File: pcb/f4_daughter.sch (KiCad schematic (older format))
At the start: 0 parts

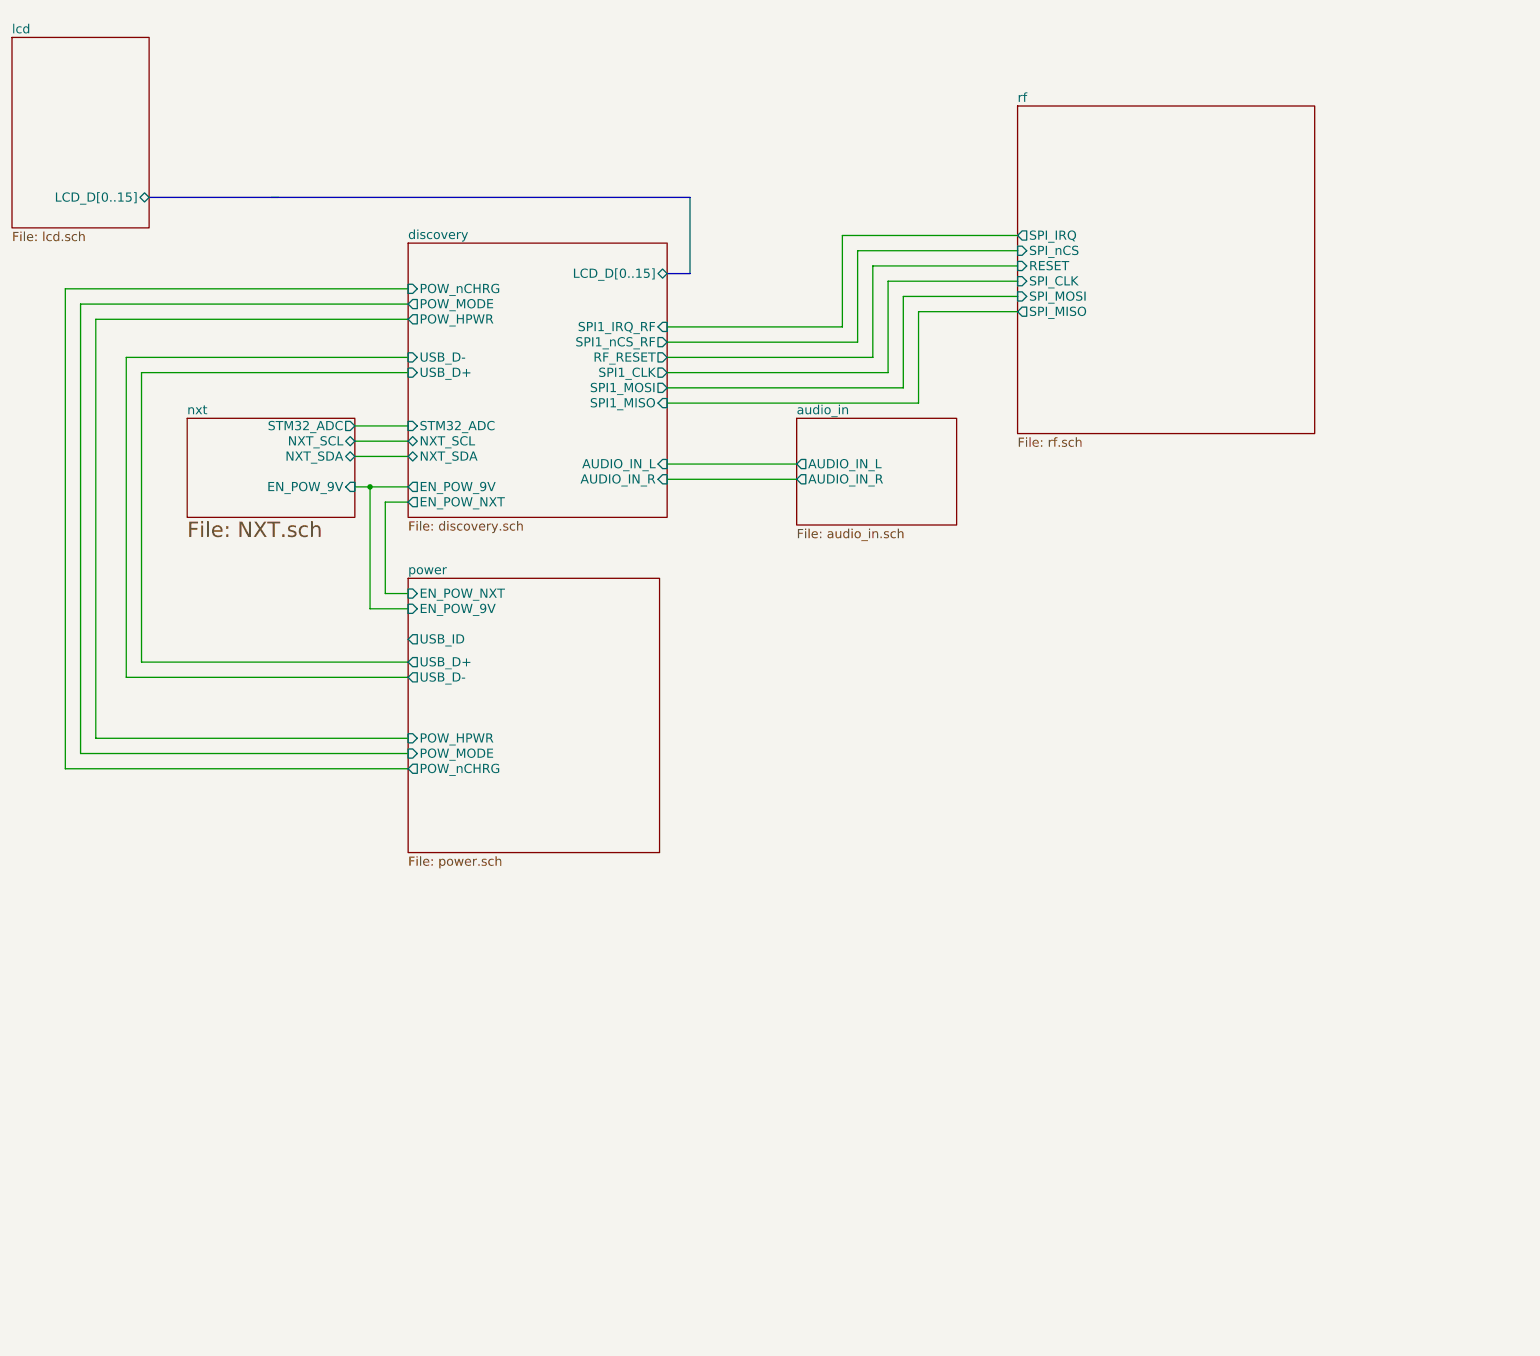
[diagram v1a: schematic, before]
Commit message: A few things: Remapped all interrupts and identified unusable pins on board Added all required connections for LCD and company Added pull-down resistor on STM32W Renamed some internal signals on RF for consistency
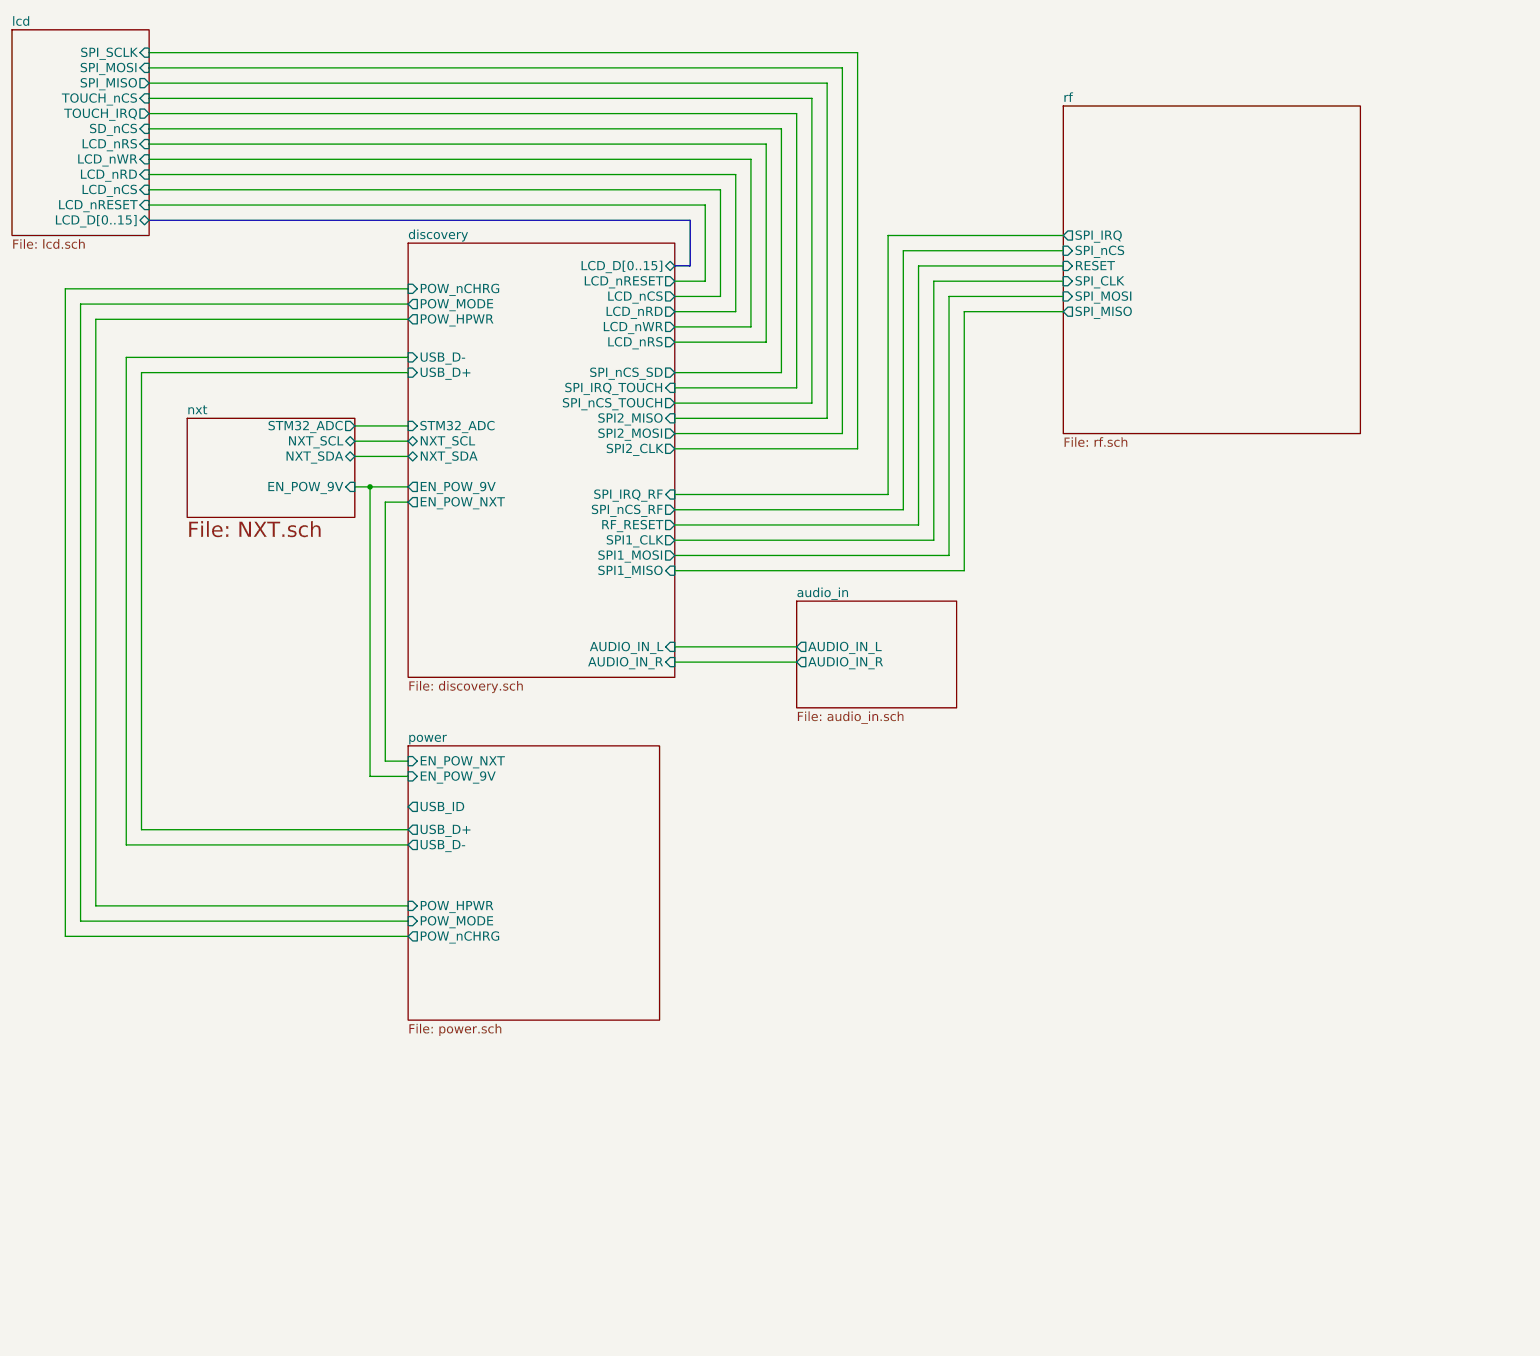
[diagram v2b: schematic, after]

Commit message: Changed some values and connected more LCD signals
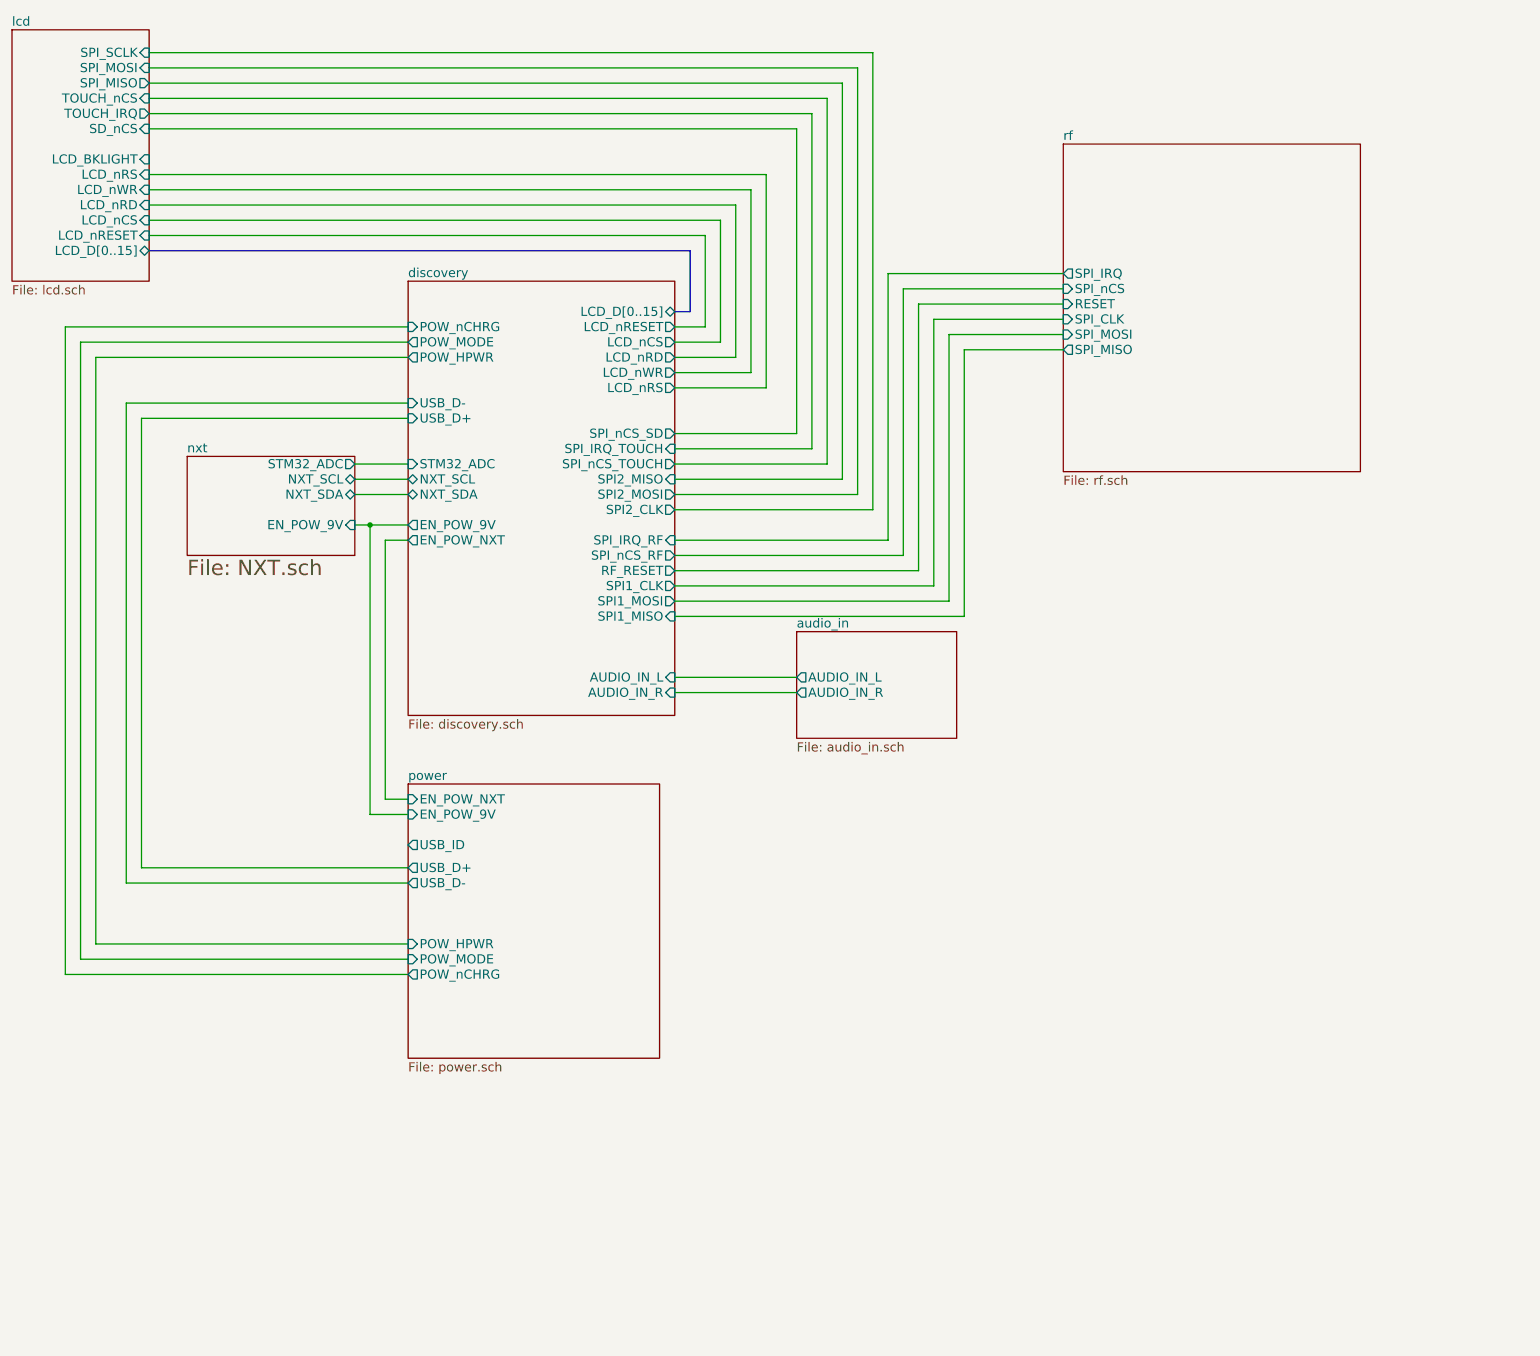
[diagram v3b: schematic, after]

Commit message: Added CPLD, CPLD doc, and backlight driver doc
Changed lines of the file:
@@
-EESchema Schematic File Version 2  date Sun 28 Oct 2012 06:31:28 PM EDT
+EESchema Schematic File Version 2  date Thu 06 Dec 2012 03:45:08 PM EST
 LIBS:power
 LIBS:device
@@
 Sheet 1 7
 Title ""
-Date "28 oct 2012"
+Date "6 dec 2012"
 Rev ""
 Comp ""
@@
 	3600 3700 3950 3700
 Wire Wire Line
-	3600 3900 3950 3900
+	3600 3900 3700 3900
+Wire Wire Line
+	3700 3900 3950 3900
 Wire Wire Line
 	2200 6150 2200 3200

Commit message: Started moving things around for CPLD
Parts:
- added S? (x4): EVQ-Q2S03W, symbol EVQ-Q2S03W
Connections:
- net labels added: GND, S1, S2, S3, S4
- wire segments 78 -> 97

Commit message: finished CPLD schematic and started adding new discovery sheet
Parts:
- removed S? (x4): EVQ-Q2S03W, symbol EVQ-Q2S03W
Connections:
- net labels removed: GND, S1, S2, S3, S4
- wire segments 97 -> 81
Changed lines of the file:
@@
-EESchema Schematic File Version 2  date Thu 06 Dec 2012 06:44:11 PM EST
+EESchema Schematic File Version 2  date 12/12/2012 5:26:02 PM
 LIBS:power
 LIBS:device
@@
 $Descr A4 11700 8267
 encoding utf-8
-Sheet 1 8
+Sheet 1 10
 Title ""
-Date "6 dec 2012"
+Date "12 dec 2012"
 Rev ""
 Comp ""
@@
 Comment4 ""
 $EndDescr
+$Sheet
+S 7900 4700 1700 4450
+U 50C8AECE
+F0 "CPLD" 60
+F1 "CPLD.sch" 60
+F2 "POW_HPWR" O R 9600 4800 60
+F3 "POW_NXT" O R 9600 4900 60
+F4 "POW_MODE" O R 9600 5000 60
+F5 "POW_9V" O R 9600 5100 60
+F6 "POW_MULT0" I L 7900 5050 60
+F7 "POW_MULT1" I L 7900 5150 60
+F8 "POW_MULT2" I L 7900 5250 60
+F9 "FSMC_A16" I L 7900 5450 60
+F10 "FSMC_NWE" I L 7900 5550 60
+F11 "FSMC_NEx" I L 7900 5650 60
+F12 "EXTI0" O L 7900 5800 60
+F13 "EXTI1" O L 7900 5900 60
+F14 "EXTI2" O L 7900 6000 60
+F15 "EXTI3" O L 7900 6100 60
+F16 "EXTI4" O L 7900 6200 60
+F17 "EXTI5" O L 7900 6300 60
+F18 "EXTI9" O L 7900 6400 60
+F19 "EXTI8" O L 7900 6500 60
+F20 "EXTI7" O L 7900 6600 60
+F21 "EXTI6" O L 7900 6700 60
+F22 "SPI_MISO" O R 9600 5350 60
+F23 "SPI_NCS" I R 9600 5450 60
+F24 "SPI_MOSI" I R 9600 5550 60
+F25 "SPI_SCK" I R 9600 5650 60
+F26 "RS" O R 9600 5800 60
+F27 "nWR" O R 9600 5900 60
+F28 "nRD" O R 9600 6000 60
+F29 "nCS" O R 9600 6150 60
+F30 "TOUCH_IRQ" I R 9600 6300 60
+F31 "RF_IRQ" I R 9600 6350 60
+F32 "DEN_GYR" I R 9600 6500 60
+F33 "INT2_GYR/DRDY" I R 9600 6600 60
+F34 "INT1_GYR" I R 9600 6750 60
+F35 "INT2_ACC" I R 9600 6850 60
+F36 "INT1_ACC" I R 9600 7000 60
+$EndSheet
 Connection ~ 7400 4300
 Wire Wire Line
-	8450 4300 5700 4300
+	9550 4250 8500 4250
+Wire Wire Line
+	7400 4300 5700 4300
 Connection ~ 7600 4500
 Wire Wire Line
-	8450 4500 5700 4500
+	9550 4450 8700 4450
+Wire Wire Line
+	7600 4500 5700 4500
 Wire Wire Line
 	7850 2350 7200 2350
@@
 	2200 3200 2200 6150
 Wire Wire Line
-	3600 3900 3950 3900
+	3600 3900 3700 3900
+Wire Wire Line
+	3700 3900 3950 3900
 Wire Wire Line
 	3600 3700 3950 3700
@@
 	7600 2750 7600 4500
 Wire Wire Line
-	10350 5075 10250 5075
-Wire Wire Line
-	10700 5275 10700 5400
-Wire Wire Line
-	10350 4725 10350 4850
-Wire Wire Line
-	10350 4850 10700 4850
-Wire Wire Line
-	10700 4850 10700 4725
-Wire Wire Line
-	10350 3925 10250 3925
-Wire Wire Line
-	10850 5825 10700 5825
-Wire Wire Line
-	10700 5275 10850 5275
-Wire Wire Line
-	10850 4125 10700 4125
-Wire Wire Line
-	10700 4725 10850 4725
-Wire Wire Line
-	10700 4125 10700 4250
-Wire Wire Line
-	10700 4250 10350 4250
-Wire Wire Line
-	10350 4250 10350 4125
-Wire Wire Line
-	10700 5400 10350 5400
-Wire Wire Line
-	10350 5400 10350 5275
-Wire Wire Line
-	10700 5825 10700 5950
-Wire Wire Line
-	10700 5950 10350 5950
-Wire Wire Line
-	10350 5950 10350 5825
-Wire Wire Line
-	10350 5625 10250 5625
-Wire Wire Line
-	10225 4525 10350 4525
-Wire Wire Line
 	7500 2650 7850 2650
 Wire Wire Line
@@
 	7100 2250 7850 2250
 Wire Wire Line
-	8450 4400 5700 4400
+	9550 4350 8600 4350
+Wire Wire Line
+	7500 4400 5700 4400
 Connection ~ 7500 4400
 $Sheet
@@
 $EndSheet
 $Sheet
-S 7850 2100 600  800
+S 8950 2050 600  800
 U 500DC44C
 F0 "rf" 60
 F1 "rf.sch" 60
-F2 "RESET" I L 7850 2450 60
-F3 "SPI_IRQ" O L 7850 2250 60
-F4 "SPI_MOSI" I L 7850 2650 60
-F5 "SPI_MISO" O L 7850 2750 60
-F6 "SPI_CLK" I L 7850 2550 60
-F7 "SPI_nCS" I L 7850 2350 60
+F2 "RESET" I L 8950 2400 60
+F3 "SPI_IRQ" O L 8950 2200 60
+F4 "SPI_MOSI" I L 8950 2600 60
+F5 "SPI_MISO" O L 8950 2700 60
+F6 "SPI_CLK" I L 8950 2500 60
+F7 "SPI_nCS" I L 8950 2300 60
 $EndSheet
 $Sheet
-S 8450 3100 1350 1800
+S 9550 3050 1350 1800
 U 50C1133E
 F0 "sensors" 60
 F1 "sensors.sch" 60
-F2 "DEN_GYR" O L 8450 3300 60
-F3 "INT2_GYR/DRDY" O L 8450 3400 60
-F4 "INT1_GYR" O L 8450 3500 60
-F5 "INT2_ACC" O L 8450 3700 60
-F6 "INT1_ACC" O L 8450 3800 60
-F7 "SPI_nCS_GYR" I L 8450 4000 60
-F8 "SPI_nCS_ACC" I L 8450 4100 60
-F9 "SPI_CLK" I L 8450 4300 60
-F10 "SPI_MOSI" I L 8450 4400 60
-F11 "SPI_MISO" O L 8450 4500 60
+F2 "DEN_GYR" O L 9550 3250 60
+F3 "INT2_GYR/DRDY" O L 9550 3350 60
+F4 "INT1_GYR" O L 9550 3450 60
+F5 "INT2_ACC" O L 9550 3650 60
+F6 "INT1_ACC" O L 9550 3750 60
+F7 "SPI_nCS_GYR" I L 9550 3950 60
+F8 "SPI_nCS_ACC" I L 9550 4050 60
+F9 "SPI_CLK" I L 9550 4250 60
+F10 "SPI_MOSI" I L 9550 4350 60
+F11 "SPI_MISO" O L 9550 4450 60
 $EndSheet
-$Comp
-L EVQ-Q2S03W S?
-U 1 1 50C112F3
-P 10525 4025
-F 0 "S?" H 10525 3850 60  0000 C CNN
-F 1 "EVQ-Q2S03W" H 10525 4250 60  0000 C CNN
-	1    10525 4025
-	1    0    0    -1
-$EndComp
-$Comp
-L EVQ-Q2S03W S?
-U 1 1 50C112F2
-P 10525 4625
-F 0 "S?" H 10525 4450 60  0000 C CNN
-F 1 "EVQ-Q2S03W" H 10525 4825 60  0000 C CNN
-	1    10525 4625
-	1    0    0    -1
-$EndComp
-$Comp
-L EVQ-Q2S03W S?
-U 1 1 50C112F1
-P 10525 5175
-F 0 "S?" H 10525 5000 60  0000 C CNN
-F 1 "EVQ-Q2S03W" H 10525 5375 60  0000 C CNN
-	1    10525 5175
-	1    0    0    -1
-$EndComp
-$Comp
-L EVQ-Q2S03W S?
-U 1 1 50C112F0
-P 10525 5725
-F 0 "S?" H 10525 5550 60  0000 C CNN
-F 1 "EVQ-Q2S03W" H 10525 5950 60  0000 C CNN
-	1    10525 5725
-	1    0    0    -1
-$EndComp
-$Comp
-L GND #PWR?
-U 1 1 50C112EF
-P 10850 4125
-F 0 "#PWR?" H 10850 4125 30  0001 C CNN
-F 1 "GND" H 10850 4055 30  0001 C CNN
-	1    10850 4125
-	0    -1   1    0
-$EndComp
-$Comp
-L GND #PWR?
-U 1 1 50C112EE
-P 10850 5275
-F 0 "#PWR?" H 10850 5275 30  0001 C CNN
-F 1 "GND" H 10850 5205 30  0001 C CNN
-	1    10850 5275
-	0    -1   1    0
-$EndComp
-$Comp
-L GND #PWR?
-U 1 1 50C112ED
-P 10850 4725
-F 0 "#PWR?" H 10850 4725 30  0001 C CNN
-F 1 "GND" H 10850 4655 30  0001 C CNN
-	1    10850 4725
-	0    -1   1    0
-$EndComp
-$Comp
-L GND #PWR?
-U 1 1 50C112EC
-P 10850 5825
-F 0 "#PWR?" H 10850 5825 30  0001 C CNN
-F 1 "GND" H 10850 5755 30  0001 C CNN
-	1    10850 5825
-	0    -1   1    0
-$EndComp
-Text Label 10250 3925 2    60   ~ 0
-S1
-Text Label 10225 4525 2    60   ~ 0
-S2
-Text Label 10250 5075 2    60   ~ 0
-S3
-Text Label 10250 5625 2    60   ~ 0
-S4
 $Sheet
 S 1350 650  900  1650
